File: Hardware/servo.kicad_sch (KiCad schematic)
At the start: 3 parts, among them J3 ServoConnector1

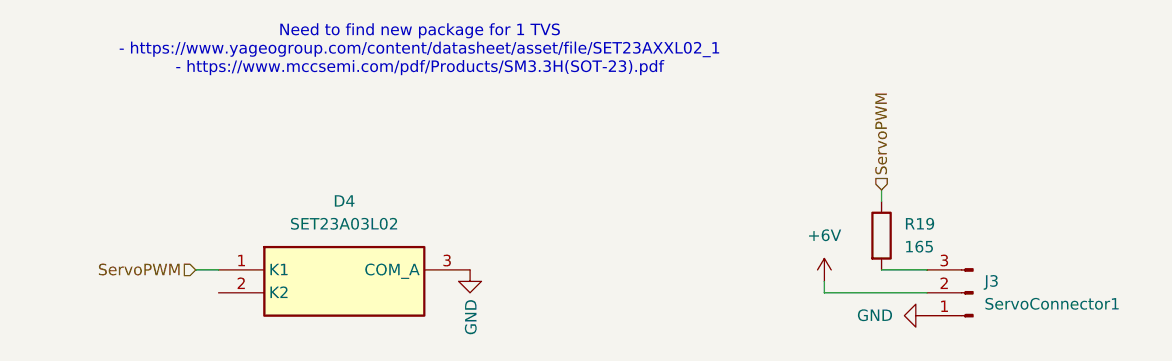
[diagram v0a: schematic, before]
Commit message: tvs diode updated
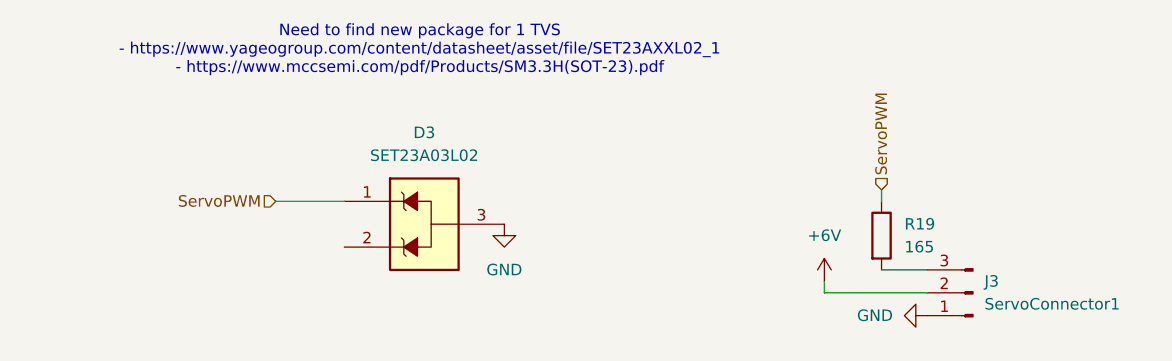
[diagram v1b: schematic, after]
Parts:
- removed D4: SET23A03L02, SOT95P230X109-3N, symbol SET23A03L02:SET23A03L02
- added D3: SET23A03L02, SOT95P230X109-3N, symbol iclr:SET23A03L02
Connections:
- net GND: now also D3.3
- net ServoPWM: now also D3.1
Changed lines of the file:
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@@
 	(wire
 		(pts
-			(xy 115.57 71.12) (xy 118.11 71.12)
+			(xy 124.46 63.5) (xy 132.08 63.5)
 		)
 		(stroke
@@
 	(hierarchical_label "ServoPWM"
 		(shape input)
-		(at 115.57 71.12 180)
+		(at 124.46 63.5 180)
 		(effects
 			(font
@@
 			)
 			(justify left)
-		)
-	)
-	(symbol
-		(lib_id "SET23A03L02:SET23A03L02")
-		(at 118.11 71.12 0)
-		(unit 1)
-		(exclude_from_sim no)
-		(in_bom yes)
-		(on_board yes)
-		(dnp no)
-		(fields_autoplaced yes)
-		(property "Reference" "D4"
-			(at 132.08 63.5 0)
-			(effects
-				(font
-					(size 1.27 1.27)
-				)
-			)
-		)
-		(property "Value" "SET23A03L02"
-			(at 132.08 66.04 0)
-			(effects
-				(font
-					(size 1.27 1.27)
-				)
-			)
-		)
-		(property "Footprint" "SOT95P230X109-3N"
-			(at 142.24 166.04 0)
-			(effects
-				(font
-					(size 1.27 1.27)
-				)
-				(justify left top)
-				(hide yes)
-			)
-		)
-		(property "Datasheet" ""
-			(at 142.24 266.04 0)
-			(effects
-				(font
-					(size 1.27 1.27)
-				)
-				(justify left top)
-				(hide yes)
-			)
-		)
-		(property "Description" "ESD Protection Diodes / TVS Diodes TVS ESD SOIC-08 3.3V 76.8V"
-			(at 118.11 71.12 0)
-			(effects
-				(font
-					(size 1.27 1.27)
-				)
-				(hide yes)
-			)
-		)
-		(property "Height" "1.09"
-			(at 142.24 466.04 0)
-			(effects
-				(font
-					(size 1.27 1.27)
-				)
-				(justify left top)
-				(hide yes)
-			)
-		)
-		(property "Mouser Part Number" "603-SET23A03L02"
-			(at 142.24 566.04 0)
-			(effects
-				(font
-					(size 1.27 1.27)
-				)
-				(justify left top)
-				(hide yes)
-			)
-		)
-		(property "Mouser Price/Stock" "https://www.mouser.co.uk/ProductDetail/YAGEO/SET23A03L02?qs=DRkmTr78QASD5DRaK8Y6sQ%3D%3D"
-			(at 142.24 666.04 0)
-			(effects
-				(font
-					(size 1.27 1.27)
-				)
-				(justify left top)
-				(hide yes)
-			)
-		)
-		(property "Manufacturer_Name" "YAGEO"
-			(at 142.24 766.04 0)
-			(effects
-				(font
-					(size 1.27 1.27)
-				)
-				(justify left top)
-				(hide yes)
-			)
-		)
-		(property "Manufacturer_Part_Number" "SET23A03L02"
-			(at 142.24 866.04 0)
-			(effects
-				(font
-					(size 1.27 1.27)
-				)
-				(justify left top)
-				(hide yes)
-			)
-		)
-		(pin "1"
-		)
-		(pin "3"
-		)
-		(pin "2"
-		)
-		(instances
-			(project ""
-				(path "/7db990e4-92e1-4f99-b4d2-435bbec1ba83/55ab0687-c91f-4545-a2ea-e93947dc2af8"
-					(reference "D4")
-					(unit 1)
-				)
-			)
 		)
 	)
@@
 	(symbol
 		(lib_id "power:GND")
-		(at 146.05 71.12 0)
+		(at 149.86 66.04 0)
 		(unit 1)
 		(exclude_from_sim no)
@@
 		(on_board yes)
 		(dnp no)
+		(fields_autoplaced yes)
 		(property "Reference" "#PWR046"
-			(at 146.05 77.47 0)
+			(at 149.86 72.39 0)
 			(effects
 				(font
@@
 		)
 		(property "Value" "GND"
-			(at 146.177 74.3712 90)
-			(effects
-				(font
-					(size 1.27 1.27)
-				)
-				(justify right)
+			(at 149.86 71.12 0)
+			(effects
+				(font
+					(size 1.27 1.27)
+				)
 			)
 		)
 		(property "Footprint" ""
-			(at 146.05 71.12 0)
+			(at 149.86 66.04 0)
 			(effects
 				(font
@@
 		)
 		(property "Datasheet" ""
-			(at 146.05 71.12 0)
-			(effects
-				(font
-					(size 1.27 1.27)
-				)
-				(hide yes)
-			)
-		)
-		(property "Description" ""
-			(at 146.05 71.12 0)
+			(at 149.86 66.04 0)
+			(effects
+				(font
+					(size 1.27 1.27)
+				)
+				(hide yes)
+			)
+		)
+		(property "Description" "Power symbol creates a global label with name \"GND\" , ground"
+			(at 149.86 66.04 0)
 			(effects
 				(font
@@
 		)
 		(instances
-			(project "RicardoTemplate"
+			(project ""
 				(path "/7db990e4-92e1-4f99-b4d2-435bbec1ba83/55ab0687-c91f-4545-a2ea-e93947dc2af8"
 					(reference "#PWR046")
 					(unit 1)
 				)
+			)
+		)
+	)
+	(symbol
+		(lib_id "iclr:SET23A03L02")
+		(at 132.08 63.5 0)
+		(unit 1)
+		(exclude_from_sim no)
+		(in_bom yes)
+		(on_board yes)
+		(dnp no)
+		(fields_autoplaced yes)
+		(property "Reference" "D3"
+			(at 140.97 55.88 0)
+			(effects
+				(font
+					(size 1.27 1.27)
+				)
+			)
+		)
+		(property "Value" "SET23A03L02"
+			(at 140.97 58.42 0)
+			(effects
+				(font
+					(size 1.27 1.27)
+				)
+			)
+		)
+		(property "Footprint" "SOT95P230X109-3N"
+			(at 156.21 158.42 0)
+			(effects
+				(font
+					(size 1.27 1.27)
+				)
+				(justify left top)
+				(hide yes)
+			)
+		)
+		(property "Datasheet" "https://www.mouser.co.uk/datasheet/3/508/1/SET23AXXL02_1.pdf"
+			(at 156.21 258.42 0)
+			(effects
+				(font
+					(size 1.27 1.27)
+				)
+				(justify left top)
+				(hide yes)
+			)
+		)
+		(property "Description" "ESD Protection Diodes / TVS Diodes TVS ESD SOIC-08 3.3V 76.8V"
+			(at 135.382 51.308 0)
+			(effects
+				(font
+					(size 1.27 1.27)
+				)
+				(hide yes)
+			)
+		)
+		(property "Height" "1.09"
+			(at 156.21 458.42 0)
+			(effects
+				(font
+					(size 1.27 1.27)
+				)
+				(justify left top)
+				(hide yes)
+			)
+		)
+		(property "Mouser Part Number" "603-SET23A03L02"
+			(at 156.21 558.42 0)
+			(effects
+				(font
+					(size 1.27 1.27)
+				)
+				(justify left top)
+				(hide yes)
+			)
+		)
+		(property "Mouser Price/Stock" "https://www.mouser.co.uk/ProductDetail/YAGEO/SET23A03L02?qs=DRkmTr78QASD5DRaK8Y6sQ%3D%3D"
+			(at 156.21 658.42 0)
+			(effects
+				(font
+					(size 1.27 1.27)
+				)
+				(justify left top)
+				(hide yes)
+			)
+		)
+		(property "Manufacturer_Name" "YAGEO"
+			(at 156.21 758.42 0)
+			(effects
+				(font
+					(size 1.27 1.27)
+				)
+				(justify left top)
+				(hide yes)
+			)
+		)
+		(property "Manufacturer_Part_Number" "SET23A03L02"
+			(at 156.21 858.42 0)
+			(effects
+				(font
+					(size 1.27 1.27)
+				)
+				(justify left top)
+				(hide yes)
+			)
+		)
+		(property "SpiceModel" ""
+			(at 160.02 46.736 0)
+			(effects
+				(font
+					(size 1.27 1.27)
+				)
+				(hide yes)
+			)
+		)
+		(property "Sim.Library" "${ICLR_HW}/spice/set23a03l02.lib"
+			(at 141.478 80.518 0)
+			(effects
+				(font
+					(size 1.27 1.27)
+				)
+				(hide yes)
+			)
+		)
+		(property "Sim.Name" "SET23A03L02_2CH"
+			(at 141.478 75.438 0)
+			(effects
+				(font
+					(size 1.27 1.27)
+				)
+				(hide yes)
+			)
+		)
+		(property "Sim.Device" "SUBCKT"
+			(at 141.478 82.55 0)
+			(effects
+				(font
+					(size 1.27 1.27)
+				)
+				(hide yes)
+			)
+		)
+		(property "Sim.Pins" "1=1 2=2 3=3"
+			(at 141.224 78.232 0)
+			(effects
+				(font
+					(size 1.27 1.27)
+				)
+				(hide yes)
+			)
+		)
+		(pin "2"
+		)
+		(pin "1"
+		)
+		(pin "3"
+		)
+		(instances
+			(project ""
+				(path "/7db990e4-92e1-4f99-b4d2-435bbec1ba83/55ab0687-c91f-4545-a2ea-e93947dc2af8"
+					(reference "D3")
+					(unit 1)
+				)
